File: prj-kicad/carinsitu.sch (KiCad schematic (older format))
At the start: 35 parts, among them P1 BAT, P2 MOT, P3 CONN_3, SW1 SWITCH_SLIDE, U1 ESP32, U2 MIC2860, U3 STC3100, U4 SN74LVC1T45, X1 40MHz

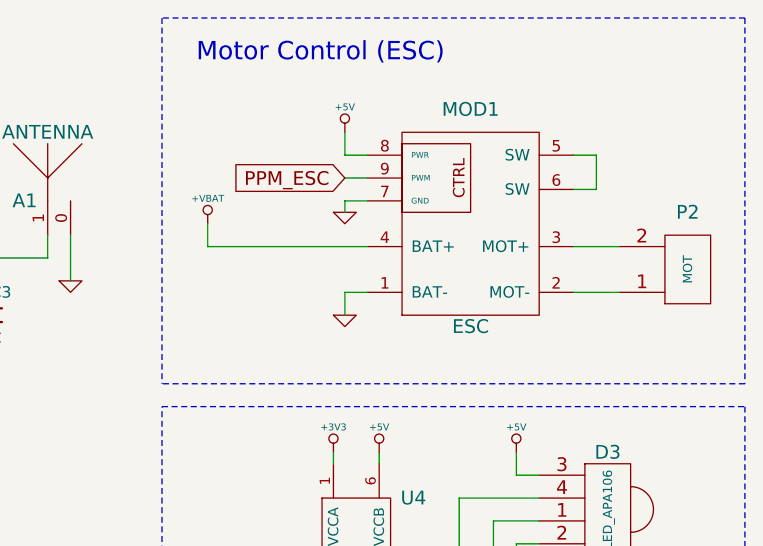
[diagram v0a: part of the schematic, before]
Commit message: = ADD: insert a 3V3 power regulator. Schematic and place ok, routing not complete
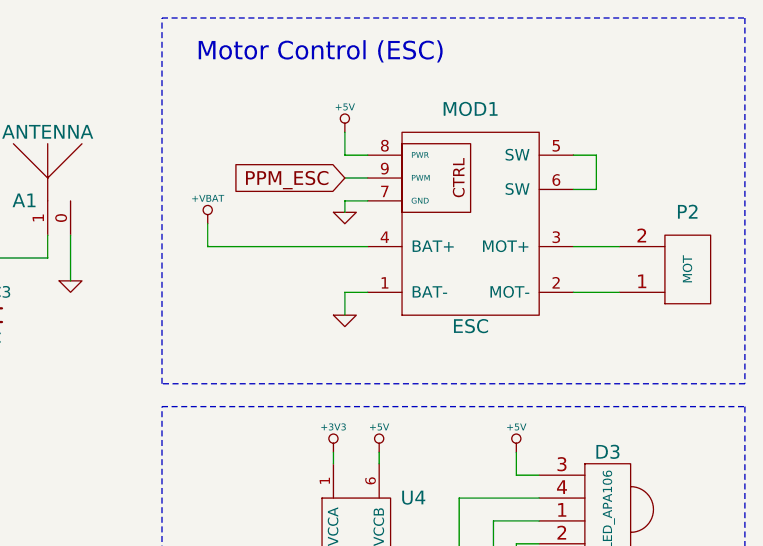
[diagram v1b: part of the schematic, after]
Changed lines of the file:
@@
 EESchema Schematic File Version 2
 LIBS:carinsitu
+LIBS:nauticsafe-gateway
 LIBS:carinsitu-cache
 EELAYER 25 0
@@
 $Descr A4 11693 8268
 encoding utf-8
-Sheet 1 1
+Sheet 1 2
 Title "Carinsitu"
 Date "2019-06-18"
@@
 NoConn ~ 2800 5250
 $Comp
-L GND #PWR025
+L GND #PWR024
 U 1 1 5D1C7B92
 P 9350 2650
-F 0 "#PWR025" H 9350 2650 30  0001 C CNN
+F 0 "#PWR024" H 9350 2650 30  0001 C CNN
 F 1 "GND" H 9350 2580 30  0001 C CNN
 F 2 "" H 9350 2650 60  0000 C CNN
@@
 	9350 2550 9450 2550
 $Comp
-L +VBAT #PWR026
+L +VBAT #PWR025
 U 1 1 5D1C7D28
 P 3850 4950
-F 0 "#PWR026" H 3850 4910 30  0001 C CNN
+F 0 "#PWR025" H 3850 4910 30  0001 C CNN
 F 1 "+VBAT" H 3850 5060 30  0000 C CNN
 F 2 "" H 3850 4950 60  0000 C CNN
@@
 	3850 5050 3850 4950
 $Comp
-L +VBAT #PWR027
+L +VBAT #PWR026
 U 1 1 5D1C8031
 P 8750 2250
-F 0 "#PWR027" H 8750 2210 30  0001 C CNN
+F 0 "#PWR026" H 8750 2210 30  0001 C CNN
 F 1 "+VBAT" H 8750 2360 30  0000 C CNN
 F 2 "" H 8750 2250 60  0000 C CNN
@@
 $EndComp
 $Comp
-L +VBAT #PWR028
+L +VBAT #PWR027
 U 1 1 5D245C91
 P 2550 5750
-F 0 "#PWR028" H 2550 5710 30  0001 C CNN
+F 0 "#PWR027" H 2550 5710 30  0001 C CNN
 F 1 "+VBAT" H 2550 5860 30  0000 C CNN
 F 2 "" H 2550 5750 60  0000 C CNN
@@
 $EndComp
 $Comp
-L GND #PWR029
+L GND #PWR028
 U 1 1 5D246224
 P 2050 7050
-F 0 "#PWR029" H 2050 7050 30  0001 C CNN
+F 0 "#PWR028" H 2050 7050 30  0001 C CNN
 F 1 "GND" H 2050 6980 30  0001 C CNN
 F 2 "" H 2050 7050 60  0000 C CNN
@@
 $EndComp
 $Comp
-L GND #PWR030
+L GND #PWR029
 U 1 1 5D246272
 P 2550 6650
-F 0 "#PWR030" H 2550 6650 30  0001 C CNN
+F 0 "#PWR029" H 2550 6650 30  0001 C CNN
 F 1 "GND" H 2550 6580 30  0001 C CNN
 F 2 "" H 2550 6650 60  0000 C CNN
@@
 Connection ~ 3250 6350
 $Comp
-L GND #PWR031
+L GND #PWR030
 U 1 1 5D247054
 P 3250 7050
-F 0 "#PWR031" H 3250 7050 30  0001 C CNN
+F 0 "#PWR030" H 3250 7050 30  0001 C CNN
 F 1 "GND" H 3250 6980 30  0001 C CNN
 F 2 "" H 3250 7050 60  0000 C CNN
@@
 	3750 5050 3750 5450
 $Comp
-L GND #PWR032
+L GND #PWR031
 U 1 1 5D247EAC
 P 3750 6600
-F 0 "#PWR032" H 3750 6600 30  0001 C CNN
+F 0 "#PWR031" H 3750 6600 30  0001 C CNN
 F 1 "GND" H 3750 6530 30  0001 C CNN
 F 2 "" H 3750 6600 60  0000 C CNN
@@
 $EndComp
 $Comp
-L +5V #PWR033
+L +5V #PWR032
 U 1 1 5D249839
 P 7700 5350
-F 0 "#PWR033" H 7700 5310 30  0001 C CNN
+F 0 "#PWR032" H 7700 5310 30  0001 C CNN
 F 1 "+5V" H 7700 5460 30  0000 C CNN
 F 2 "" H 7700 5350 60  0000 C CNN
@@
 $EndComp
 $Comp
-L GND #PWR034
+L GND #PWR033
 U 1 1 5D24995A
 P 7700 5950
-F 0 "#PWR034" H 7700 5950 30  0001 C CNN
+F 0 "#PWR033" H 7700 5950 30  0001 C CNN
 F 1 "GND" H 7700 5880 30  0001 C CNN
 F 2 "" H 7700 5950 60  0000 C CNN
@@
 $EndComp
 $Comp
-L +5V #PWR035
+L +5V #PWR034
 U 1 1 5D24AFFE
 P 10100 3250
-F 0 "#PWR035" H 10100 3210 30  0001 C CNN
+F 0 "#PWR034" H 10100 3210 30  0001 C CNN
 F 1 "+5V" H 10100 3360 30  0000 C CNN
 F 2 "" H 10100 3250 60  0000 C CNN
@@
 	10100 3650 10200 3650
 $Comp
-L GND #PWR036
+L GND #PWR035
 U 1 1 5D24B1A0
 P 10100 3750
-F 0 "#PWR036" H 10100 3750 30  0001 C CNN
+F 0 "#PWR035" H 10100 3750 30  0001 C CNN
 F 1 "GND" H 10100 3680 30  0001 C CNN
 F 2 "" H 10100 3750 60  0000 C CNN
@@
 $EndComp
 $Comp
-L +5V #PWR037
+L +5V #PWR036
 U 1 1 5D24B240
 P 10100 4000
-F 0 "#PWR037" H 10100 3960 30  0001 C CNN
+F 0 "#PWR036" H 10100 3960 30  0001 C CNN
 F 1 "+5V" H 10100 4110 30  0000 C CNN
 F 2 "" H 10100 4000 60  0000 C CNN
@@
 	10100 4400 10200 4400
 $Comp
-L GND #PWR038
+L GND #PWR037
 U 1 1 5D24B465
 P 10100 4500
-F 0 "#PWR038" H 10100 4500 30  0001 C CNN
+F 0 "#PWR037" H 10100 4500 30  0001 C CNN
 F 1 "GND" H 10100 4430 30  0001 C CNN
 F 2 "" H 10100 4500 60  0000 C CNN
@@
 	9700 3750 9850 3750
 $Comp
-L +5V #PWR039
+L +5V #PWR038
 U 1 1 5D24BD16
 P 9500 3250
-F 0 "#PWR039" H 9500 3210 30  0001 C CNN
+F 0 "#PWR038" H 9500 3210 30  0001 C CNN
 F 1 "+5V" H 9500 3360 30  0000 C CNN
 F 2 "" H 9500 3250 60  0000 C CNN
@@
 $EndComp
 $Comp
-L +3V3 #PWR040
+L +3V3 #PWR039
 U 1 1 5D24BED7
 P 9300 3250
-F 0 "#PWR040" H 9300 3210 30  0001 C CNN
+F 0 "#PWR039" H 9300 3210 30  0001 C CNN
 F 1 "+3V3" H 9300 3360 30  0000 C CNN
 F 2 "" H 9300 3250 60  0000 C CNN
@@
 	9850 3450 10200 3450
 $Comp
-L GND #PWR041
+L GND #PWR040
 U 1 1 5D24C2F7
 P 9400 4250
-F 0 "#PWR041" H 9400 4250 30  0001 C CNN
+F 0 "#PWR040" H 9400 4250 30  0001 C CNN
 F 1 "GND" H 9400 4180 30  0001 C CNN
 F 2 "" H 9400 4250 60  0000 C CNN
@@
 	9050 3750 9100 3750
 $Comp
-L +3V3 #PWR042
+L +3V3 #PWR041
 U 1 1 5D24CD9B
 P 8900 4000
-F 0 "#PWR042" H 8900 3960 30  0001 C CNN
+F 0 "#PWR041" H 8900 3960 30  0001 C CNN
 F 1 "+3V3" H 8900 4110 30  0000 C CNN
 F 2 "" H 8900 4000 60  0000 C CNN
@@
 	11100 2950 8550 2950
 Wire Notes Line
-	8550 1350 8550 2950
+	8550 2950 8550 1350
 Wire Notes Line
 	11100 1350 11100 2950
 Wire Notes Line
-	11100 1350 8550 1350
+	8550 1350 11100 1350
 Text Notes 8700 1550 0    80   ~ 0
 Motor Control (ESC)

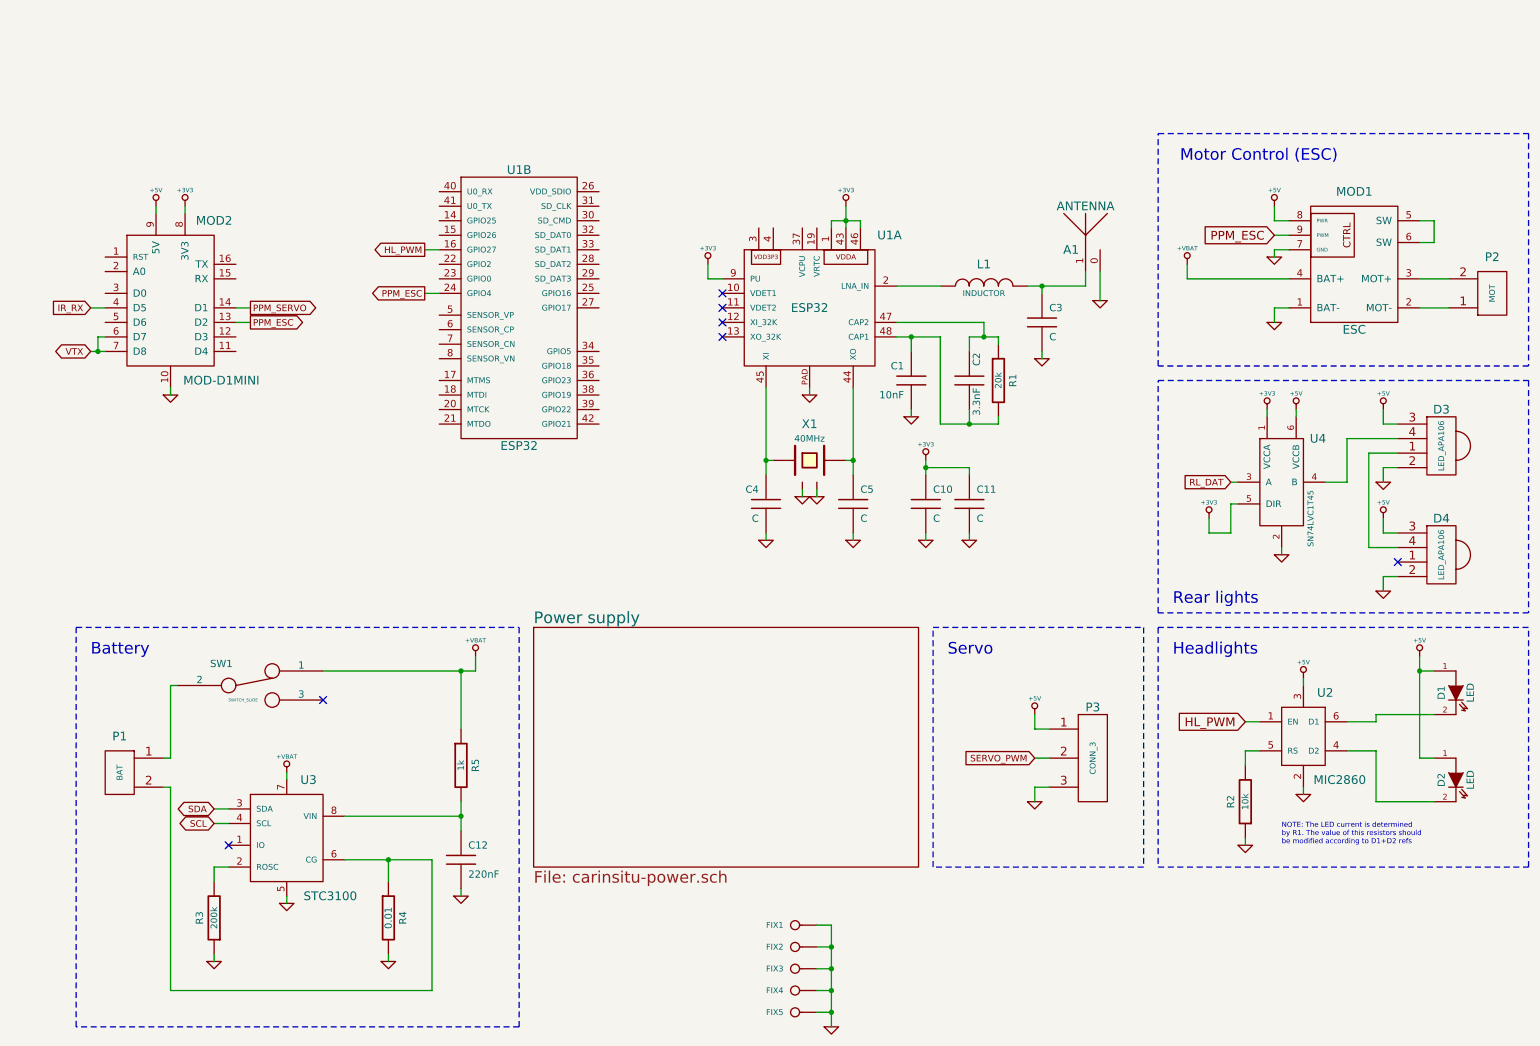
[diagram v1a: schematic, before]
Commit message: = ADD: insert iNEMO inertial chip (LSM6DS3) - Routing not complete
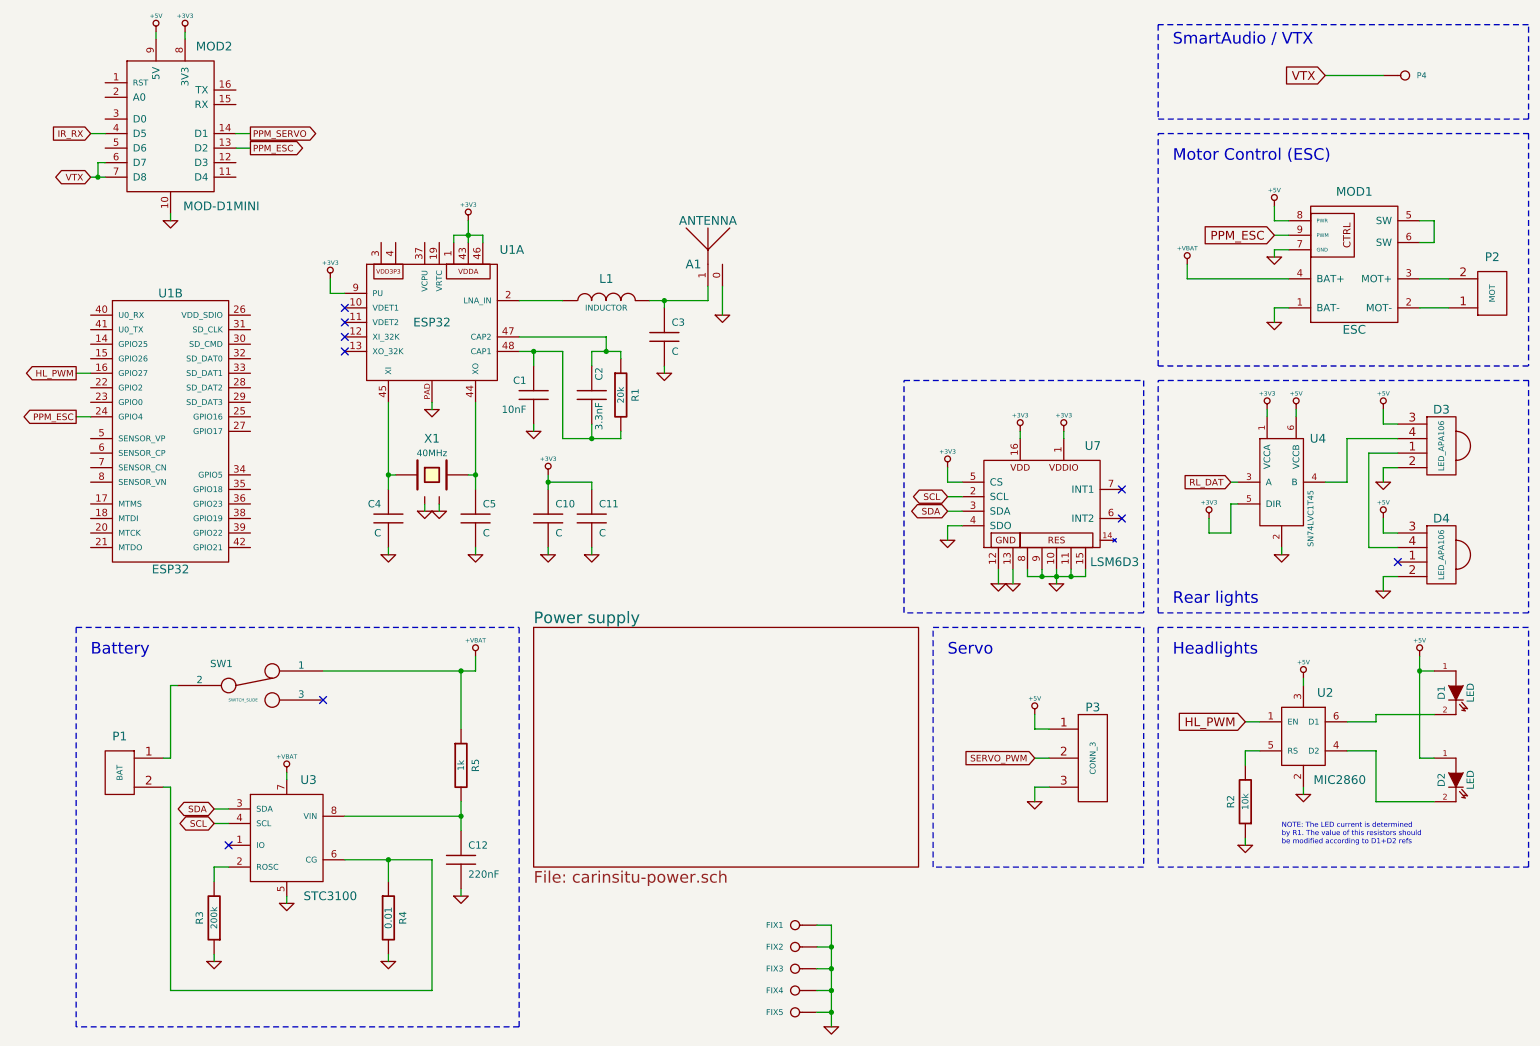
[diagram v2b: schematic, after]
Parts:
- added P4: CONN_1, symbol CONN_1
- added U7: LSM6D3, carinsitu:LGA-16, symbol LSM6D3
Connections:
- net +3V3: now also U7.1, U7.16, U7.5 (CS)
- net GND: now also U7.10, U7.11, U7.12, U7.13, U7.15, U7.4 (SDO), U7.8, U7.9
- net SCL: now also U7.2 (SCL)
- net SDA: now also U7.3 (SDA)
- net VTX: now also P4.1
- no-connect marks 7 -> 9
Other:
- note added: "SmartAudio / VTX"
- moved on the sheet: A1, C1, C10, C11, C2, C3, C4, C5, L1, MOD2, R1, U1A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

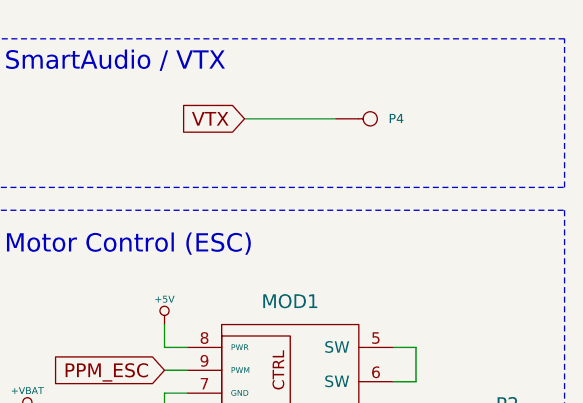
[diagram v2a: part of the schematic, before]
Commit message: = UPD: Improve RGB LED position (according to CAD specs) and power routing
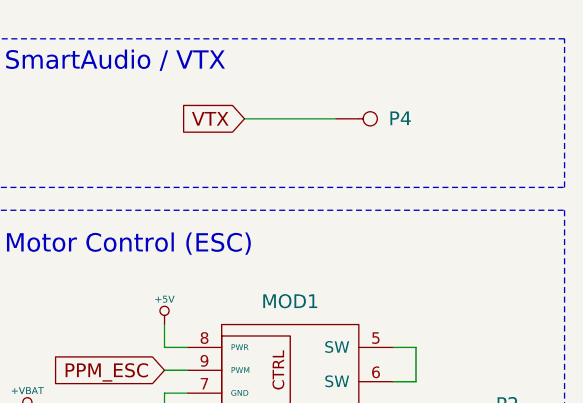
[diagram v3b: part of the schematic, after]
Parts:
- P4: footprint (none) -> carinsitu:TP
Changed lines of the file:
@@
 U 1 1 5D254928
 P 10250 950
-F 0 "P4" H 10330 950 40  0000 L CNN
+F 0 "P4" H 10330 950 60  0000 L CNN
 F 1 "CONN_1" H 10250 1005 30  0001 C CNN
-F 2 "" H 10250 950 60  0001 C CNN
+F 2 "carinsitu:TP" H 10250 950 60  0001 C CNN
 F 3 "" H 10250 950 60  0000 C CNN
 	1    10250 950
